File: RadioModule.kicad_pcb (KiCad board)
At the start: 2 copper layers, 16 x 16 mm, 33 parts, among them J1 Conn_01x01_Pin, J10 Conn_01x01_Pin, J11 Conn_01x01_Pin, J12 Conn_01x01_Pin, J13 Conn_01x01_Pin, J14 Conn_01x01_Pin, J15 Conn_01x01_Pin, J16 Conn_01x01_Pin, J2 Conn_01x01_Pin, J3 Conn_01x01_Pin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

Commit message: Post Board Review Update
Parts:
- removed C10, C8, C9: 100nF, Capacitor_SMD:C_0402_1005Metric
- added C12: 100nF, Capacitor_SMD:C_0402_1005Metric, F.Cu at (95.2, 72.3)
- added C13: 100nF, Capacitor_SMD:C_0402_1005Metric, F.Cu at (93.2, 72.7)
- added C14: 100nF, Capacitor_SMD:C_0402_1005Metric, F.Cu at (92.8, 71.0)
- L1: footprint Inductor_SMD:L_0402_1005Metric -> Inductor_SMD:L_0805_2012Metric
- moved C11 6.11 mm to (100.0, 73.0), turned to 0 degrees
- moved C7 3.37 mm to (97.0, 73.4), turned to 90 degrees
- moved L3 1.69 mm to (95.2, 71.0)
- moved L2 1.01 mm to (98.3, 73.5), turned to 90 degrees
- moved C5 0.80 mm to (97.6, 82.3)
- moved R1 0.77 mm to (97.6, 81.3)
- moved L1 0.22 mm to (100.4, 81.7)
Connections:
- C11 pad 1: Net-(C10-Pad1) -> Net-(C11-Pad1)
- J10 pad 1: unconnected-(J10-Pin_1-Pad1) -> DIO5
- J3 pad 1: unconnected-(J3-Pin_1-Pad1) -> DIO3
- J4 pad 1: unconnected-(J4-Pin_1-Pad1) -> DIO4
- J7 pad 1: unconnected-(J7-Pin_1-Pad1) -> DIO1
- J8 pad 1: unconnected-(J8-Pin_1-Pad1) -> DIO2
- L2 pad 2: Net-(C10-Pad2) -> Net-(C11-Pad1)
- L3 pad 1: Net-(C10-Pad2) -> Net-(C11-Pad1)
- L3 pad 2: Net-(C10-Pad1) -> Net-(C12-Pad1)
- U1 pad 10: unconnected-(U1-DIO3-Pad10) -> DIO3
- U1 pad 9: unconnected-(U1-DIO2-Pad9) -> DIO2
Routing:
- net DIO3: track 0.00 -> 12.0 mm, vias 0 -> 2
- net DIO2: track 0.00 -> 11.6 mm, vias 0 -> 2
- net GND: track 35.6 -> 28.2 mm, vias 9 -> 29
- net Net-(C11-Pad1): track 0.00 -> 6.19 mm
- net Net-(C12-Pad1): track 0.00 -> 3.82 mm
- net Net-(C10-Pad2): track 3.52 -> 0.00 mm
- net Net-(C10-Pad1): track 3.45 -> 0.00 mm
- net NRST: track 16.7 -> 14.2 mm, vias 4 -> 2
- net Net-(U1-VBAT_IO): track 3.14 -> 0.71 mm
- net Net-(U1-RFIO): track 4.49 -> 2.27 mm
- net ANT: track 4.44 -> 2.31 mm
- net MISO: track 10.7 -> 9.49 mm
- net 3V3: track 27.3 -> 28.3 mm
- net /V_DCC: track 25.6 -> 25.0 mm
- added copper zone on F.Cu, net /XTA
- added copper zone on F.Cu, net /XTB_Reference Oscillator
- added copper zone on F.Cu, net 3V3
- added copper zone on In2.Cu, net 3V3
- added copper zone on F.Cu, net ANT
- added copper zone on F.Cu, net GND
- added copper zone on In1.Cu, net GND
- added copper zone on F.Cu, net Net-(C11-Pad1)
- added copper zone on F.Cu, net Net-(C12-Pad1)
- added copper zone on F.Cu, net Net-(U1-RFIO)
- removed copper zone on B.Cu, net GND
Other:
- copper layers 2 -> 4
- board text added: "1"
- board text added: "DIO2"
- board text added: "DIO3"

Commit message: lets try that again
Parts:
- added C8: 100nF, Capacitor_SMD:C_0402_1005Metric, F.Cu at (103.5, 80.0)
- C11, C13: value 100nF -> 1.2pF
- C12: value 100nF -> 0.5pF
- C14: value 100nF -> 100pF
- C7: value 100nF -> 0.8pF
- L2: value 15uH -> 3nH
- L3: value 15uH -> 2.5nH
- moved C2 1.13 mm to (94.3, 75.1), turned to 90 degrees
- moved C3 0.95 mm to (93.7, 81.2)
- moved Y1 0.94 mm to (93.6, 79.3)
- moved C4 0.44 mm to (93.7, 77.4), turned to 180 degrees
- moved L1 0.37 mm to (100.8, 81.7)
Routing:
- net 3V3: track 28.3 -> 6.02 mm
- net DIO3: track 12.0 -> 21.2 mm
- net GND: track 28.2 -> 19.4 mm, vias 29 -> 37
- net NRST: track 14.2 -> 19.7 mm
- net Net-(U1-VBAT_IO): track 0.71 -> 3.91 mm
- net /XTA: track 4.08 -> 6.53 mm
- net /V_DCC: track 25.0 -> 23.2 mm
- net /XTB_Reference Oscillator: track 3.11 -> 4.67 mm
- net MOSI: track 8.87 -> 7.54 mm
- net MISO: track 9.49 -> 10.8 mm
- net SCK: track 6.85 -> 7.94 mm
- removed copper zone on F.Cu, net /XTB_Reference Oscillator
- removed copper zone on F.Cu, net 3V3

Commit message: made it less clapped
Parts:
- moved C8 2.50 mm to (102.4, 77.8), turned to 180 degrees
- moved L1 0.79 mm to (100.5, 81.0), turned to 45 degrees
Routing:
- net DIO3: track 21.2 -> 16.1 mm
- net 3V3: track 6.02 -> 3.19 mm
- net MOSI: track 7.54 -> 9.93 mm
- net /V_DCC2: track 4.70 -> 2.97 mm
- net NRST: track 19.7 -> 18.4 mm
- net DIO2: track 11.1 -> 12.3 mm
- net MISO: track 10.8 -> 12.0 mm
- net GND: vias 37 -> 33

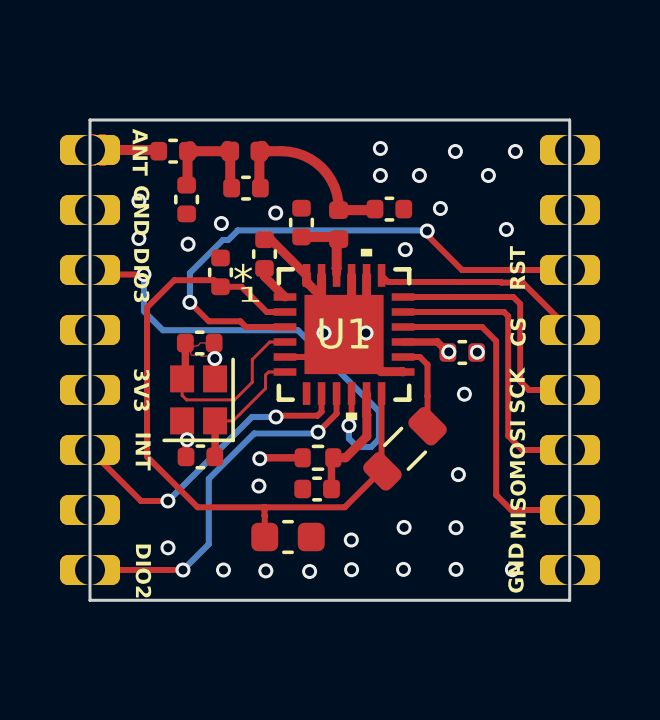
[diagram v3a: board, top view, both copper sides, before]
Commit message: Added silkscreen and changed pi filter component values
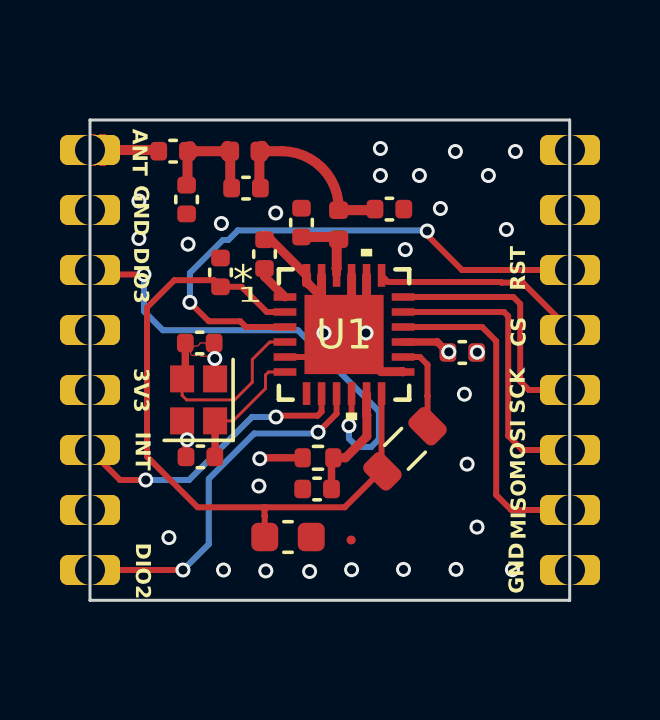
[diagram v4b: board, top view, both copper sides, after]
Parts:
- added G***: LOGO, LOGO, B.Cu at (98.5, 77.1)
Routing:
- net INT: track 10.3 -> 9.68 mm
- net GND: vias 33 -> 31
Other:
- board text added: "Designed By Soham More Electronics 2024"
- board text added: "SX1280 Module"

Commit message: Hopefully final commit
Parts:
- moved C6 2.17 mm to (94.4, 83.7), turned to -90 degrees
- moved C1 0.38 mm to (95.5, 74.4)
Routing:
- net GND: track 19.4 -> 17.4 mm, vias 31 -> 20
- net DIO2: track 12.3 -> 11.0 mm, vias 2 -> 1
- net /V_DCC: track 23.0 -> 22.0 mm
- net INT: track 9.68 -> 8.85 mm, vias 2 -> 1
- net SCK: track 8.36 -> 7.83 mm
- net DIO3: track 16.1 -> 15.6 mm, vias 2 -> 1
- added copper zone on B.Cu, net GND
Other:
- board size 16 x 16 mm -> 16 x 18 mm

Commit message: looks good
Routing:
- net GND: track 17.4 -> 2.46 mm, vias 20 -> 19
- net MISO: track 12.0 -> 9.89 mm
- net MOSI: track 9.54 -> 8.55 mm
- net SCK: track 7.83 -> 6.97 mm
- net 3V3: track 3.19 -> 3.92 mm
